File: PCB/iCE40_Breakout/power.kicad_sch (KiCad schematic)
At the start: 18 parts, among them U3 MIC5504-2.5YM5, U4 MIC5504-1.2YM5, U5 MIC5504-3.3YM5, U6 MIC5504-3.3YM5

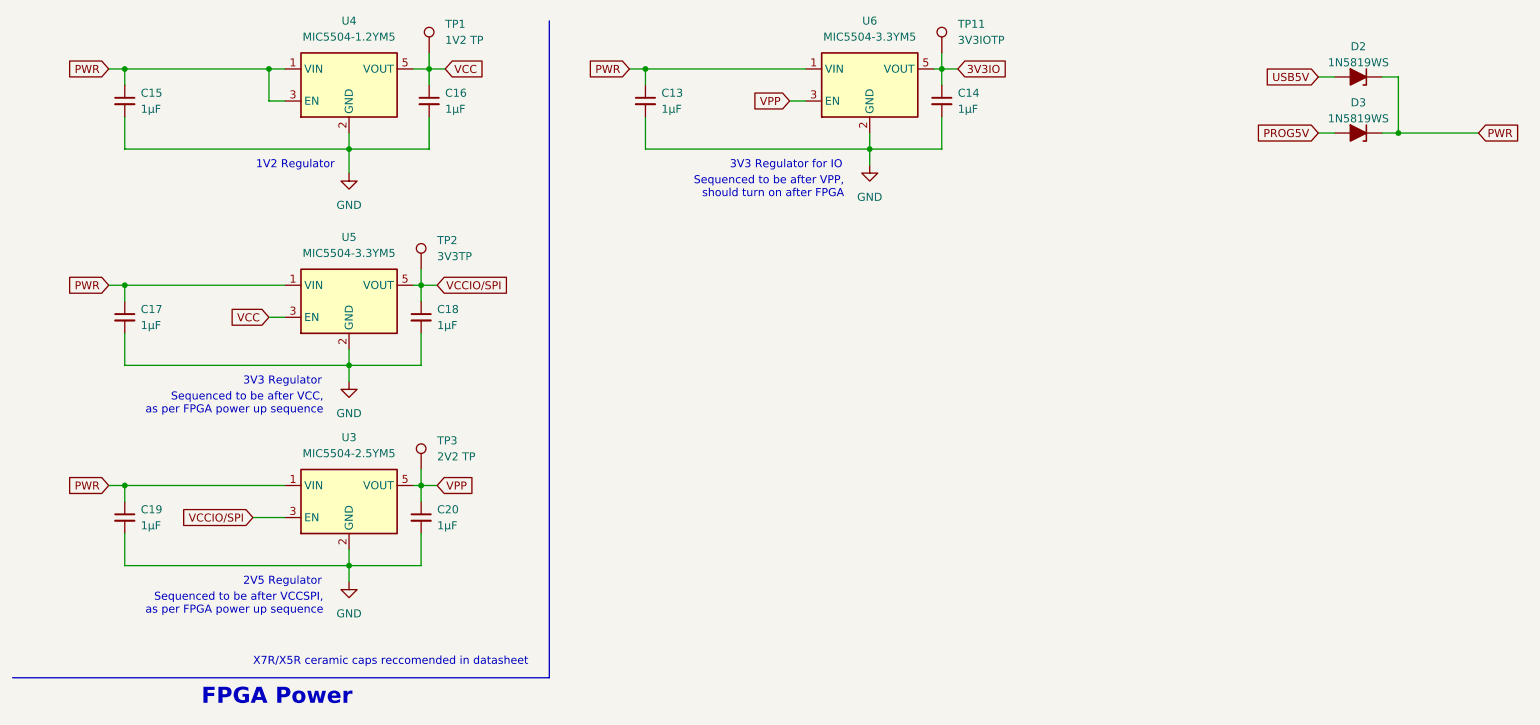
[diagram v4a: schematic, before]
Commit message: Wired FTDI chip to flash memory, and added power connections
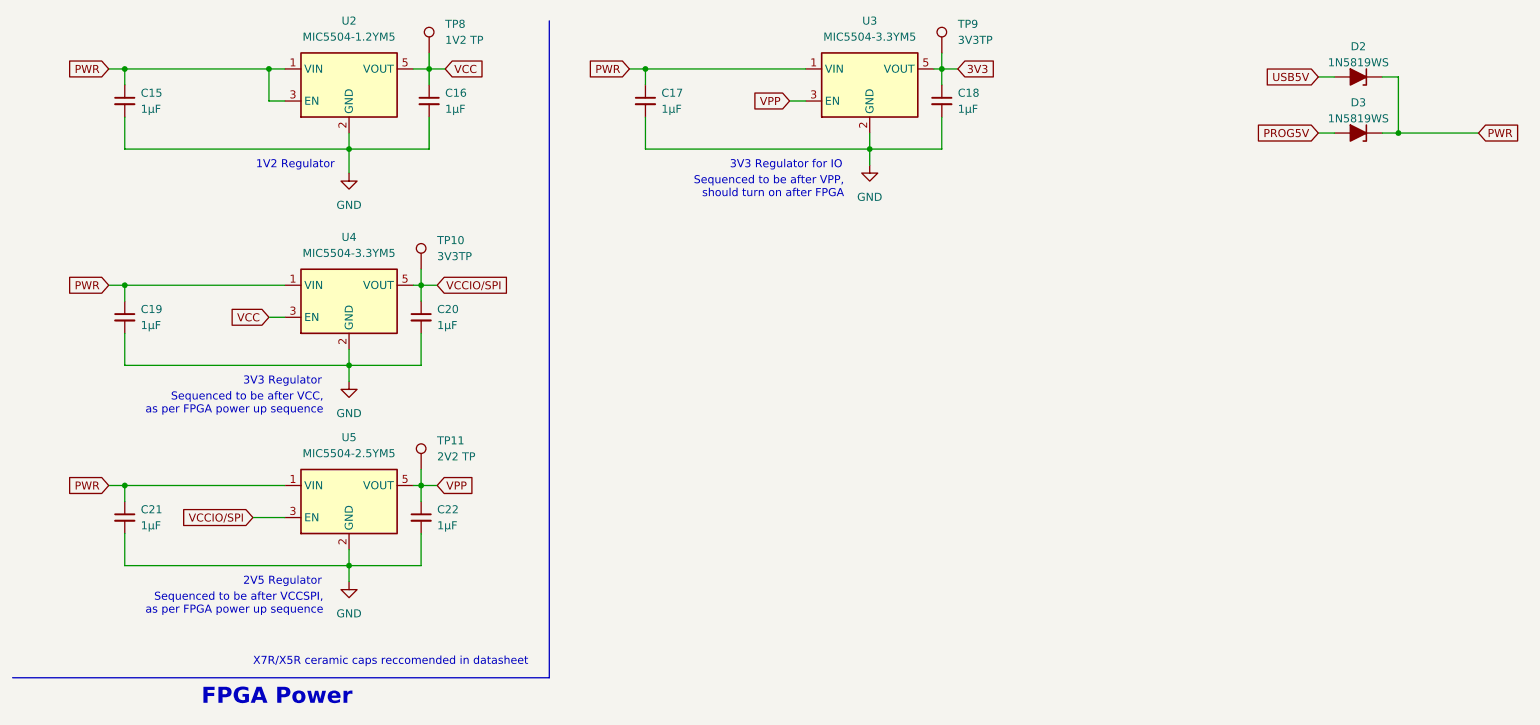
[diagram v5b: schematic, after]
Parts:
- TP9: renamed from TP11; value 3V3IOTP -> 3V3TP
- renumbered C13 to C17, C14 to C18, C17 to C19, C18 to C20, C19 to C21, C20 to C22, TP2 to TP10, TP3 to TP11, TP1 to TP8, U4 to U2, U6 to U3, U5 to U4, U3 to U5
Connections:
- net 3V3IO renamed 3V3
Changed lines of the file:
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@@
 		)
 	)
-	(global_label "3V3IO"
+	(global_label "3V3"
 		(shape input)
 		(at 165.1 21.59 0)
@@
 		(dnp no)
 		(fields_autoplaced yes)
-		(property "Reference" "C20"
+		(property "Reference" "C22"
 			(at 82.55 91.4462 0)
 			(effects
@@
 			(project "iCE40_Breakout"
 				(path "/ce4d7974-ef38-4eea-8119-381c4298ef02/01a0af1d-1c95-48f8-8e55-14d3b3651b87"
-					(reference "C20")
+					(reference "C22")
 					(unit 1)
 				)
@@
 		(dnp no)
 		(fields_autoplaced yes)
-		(property "Reference" "U3"
+		(property "Reference" "U5"
 			(at 68.58 80.01 0)
 			(effects
@@
 			(project "iCE40_Breakout"
 				(path "/ce4d7974-ef38-4eea-8119-381c4298ef02/01a0af1d-1c95-48f8-8e55-14d3b3651b87"
-					(reference "U3")
+					(reference "U5")
 					(unit 1)
 				)
@@
 		(dnp no)
 		(fields_autoplaced yes)
-		(property "Reference" "C18"
+		(property "Reference" "C20"
 			(at 82.55 59.6962 0)
 			(effects
@@
 			(project "iCE40_Breakout"
 				(path "/ce4d7974-ef38-4eea-8119-381c4298ef02/01a0af1d-1c95-48f8-8e55-14d3b3651b87"
-					(reference "C18")
+					(reference "C20")
 					(unit 1)
 				)
@@
 		(on_board yes)
 		(dnp no)
-		(property "Reference" "TP3"
+		(property "Reference" "TP11"
 			(at 82.55 80.5179 0)
 			(effects
@@
 			(project "iCE40_Breakout"
 				(path "/ce4d7974-ef38-4eea-8119-381c4298ef02/01a0af1d-1c95-48f8-8e55-14d3b3651b87"
-					(reference "TP3")
+					(reference "TP11")
 					(unit 1)
 				)
@@
 		(dnp no)
 		(fields_autoplaced yes)
-		(property "Reference" "U4"
+		(property "Reference" "U2"
 			(at 68.58 13.97 0)
 			(effects
@@
 			(project "iCE40_Breakout"
 				(path "/ce4d7974-ef38-4eea-8119-381c4298ef02/01a0af1d-1c95-48f8-8e55-14d3b3651b87"
-					(reference "U4")
+					(reference "U2")
 					(unit 1)
 				)
@@
 		(dnp no)
 		(fields_autoplaced yes)
-		(property "Reference" "C13"
+		(property "Reference" "C17"
 			(at 118.11 25.4062 0)
 			(effects
@@
 			(project "iCE40_Breakout"
 				(path "/ce4d7974-ef38-4eea-8119-381c4298ef02/01a0af1d-1c95-48f8-8e55-14d3b3651b87"
-					(reference "C13")
+					(reference "C17")
 					(unit 1)
 				)
@@
 		(dnp no)
 		(fields_autoplaced yes)
-		(property "Reference" "U5"
+		(property "Reference" "U4"
 			(at 68.58 48.26 0)
 			(effects
@@
 			(project "iCE40_Breakout"
 				(path "/ce4d7974-ef38-4eea-8119-381c4298ef02/01a0af1d-1c95-48f8-8e55-14d3b3651b87"
-					(reference "U5")
+					(reference "U4")
 					(unit 1)
 				)
@@
 		(dnp no)
 		(fields_autoplaced yes)
-		(property "Reference" "#PWR017"
+		(property "Reference" "#PWR020"
 			(at 68.58 44.45 0)
 			(effects
@@
 			(project "iCE40_Breakout"
 				(path "/ce4d7974-ef38-4eea-8119-381c4298ef02/01a0af1d-1c95-48f8-8e55-14d3b3651b87"
-					(reference "#PWR017")
+					(reference "#PWR020")
 					(unit 1)
 				)
@@
 		(on_board yes)
 		(dnp no)
-		(property "Reference" "TP2"
+		(property "Reference" "TP10"
 			(at 82.55 48.7679 0)
 			(effects
@@
 			(project ""
 				(path "/ce4d7974-ef38-4eea-8119-381c4298ef02/01a0af1d-1c95-48f8-8e55-14d3b3651b87"
-					(reference "TP2")
+					(reference "TP10")
 					(unit 1)
 				)
@@
 		(dnp no)
 		(fields_autoplaced yes)
-		(property "Reference" "#PWR019"
+		(property "Reference" "#PWR021"
 			(at 68.58 77.47 0)
 			(effects
@@
 			(project "iCE40_Breakout"
 				(path "/ce4d7974-ef38-4eea-8119-381c4298ef02/01a0af1d-1c95-48f8-8e55-14d3b3651b87"
-					(reference "#PWR019")
+					(reference "#PWR021")
 					(unit 1)
 				)
@@
 		(dnp no)
 		(fields_autoplaced yes)
-		(property "Reference" "#PWR018"
+		(property "Reference" "#PWR022"
 			(at 68.58 109.22 0)
 			(effects
@@
 			(project "iCE40_Breakout"
 				(path "/ce4d7974-ef38-4eea-8119-381c4298ef02/01a0af1d-1c95-48f8-8e55-14d3b3651b87"
-					(reference "#PWR018")
+					(reference "#PWR022")
 					(unit 1)
 				)
@@
 		(dnp no)
 		(fields_autoplaced yes)
-		(property "Reference" "#PWR023"
+		(property "Reference" "#PWR019"
 			(at 151.13 43.18 0)
 			(effects
@@
 			(project "iCE40_Breakout"
 				(path "/ce4d7974-ef38-4eea-8119-381c4298ef02/01a0af1d-1c95-48f8-8e55-14d3b3651b87"
-					(reference "#PWR023")
+					(reference "#PWR019")
 					(unit 1)
 				)
@@
 		(dnp no)
 		(fields_autoplaced yes)
-		(property "Reference" "U6"
+		(property "Reference" "U3"
 			(at 151.13 13.97 0)
 			(effects
@@
 			(project "iCE40_Breakout"
 				(path "/ce4d7974-ef38-4eea-8119-381c4298ef02/01a0af1d-1c95-48f8-8e55-14d3b3651b87"
-					(reference "U6")
+					(reference "U3")
 					(unit 1)
 				)
@@
 		(dnp no)
 		(fields_autoplaced yes)
-		(property "Reference" "C19"
+		(property "Reference" "C21"
 			(at 35.56 91.4462 0)
 			(effects
@@
 			(project "iCE40_Breakout"
 				(path "/ce4d7974-ef38-4eea-8119-381c4298ef02/01a0af1d-1c95-48f8-8e55-14d3b3651b87"
-					(reference "C19")
+					(reference "C21")
 					(unit 1)
 				)
@@
 		(on_board yes)
 		(dnp no)
-		(property "Reference" "TP11"
+		(property "Reference" "TP9"
 			(at 165.1 14.4779 0)
 			(effects
@@
 			)
 		)
-		(property "Value" "3V3IOTP"
+		(property "Value" "3V3TP"
 			(at 165.1 17.0179 0)
 			(effects
@@
 			(project "iCE40_Breakout"
 				(path "/ce4d7974-ef38-4eea-8119-381c4298ef02/01a0af1d-1c95-48f8-8e55-14d3b3651b87"
-					(reference "TP11")
+					(reference "TP9")
 					(unit 1)
 				)
@@
 		(on_board yes)
 		(dnp no)
-		(property "Reference" "TP1"
+		(property "Reference" "TP8"
 			(at 83.82 14.4779 0)
 			(effects
@@
 			(project "iCE40_Breakout"
 				(path "/ce4d7974-ef38-4eea-8119-381c4298ef02/01a0af1d-1c95-48f8-8e55-14d3b3651b87"
-					(reference "TP1")
+					(reference "TP8")
 					(unit 1)
 				)
@@
 		(dnp no)
 		(fields_autoplaced yes)
-		(property "Reference" "C14"
+		(property "Reference" "C18"
 			(at 165.1 25.4062 0)
 			(effects
@@
 			(project "iCE40_Breakout"
 				(path "/ce4d7974-ef38-4eea-8119-381c4298ef02/01a0af1d-1c95-48f8-8e55-14d3b3651b87"
-					(reference "C14")
+					(reference "C18")
 					(unit 1)
 				)
@@
 		(dnp no)
 		(fields_autoplaced yes)
-		(property "Reference" "C17"
+		(property "Reference" "C19"
 			(at 35.56 59.6962 0)
 			(effects
@@
 			(project "iCE40_Breakout"
 				(path "/ce4d7974-ef38-4eea-8119-381c4298ef02/01a0af1d-1c95-48f8-8e55-14d3b3651b87"
-					(reference "C17")
-					(unit 1)
-				)
+					(reference "C19")
+					(unit 1)
+				)

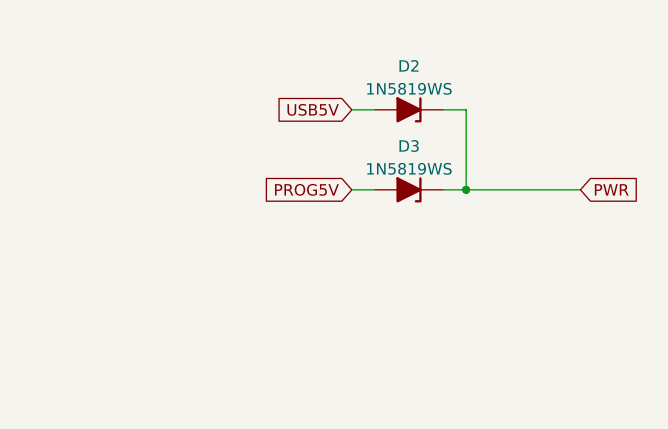
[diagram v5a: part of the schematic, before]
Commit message: Added sheet information, and fixed ERC errors
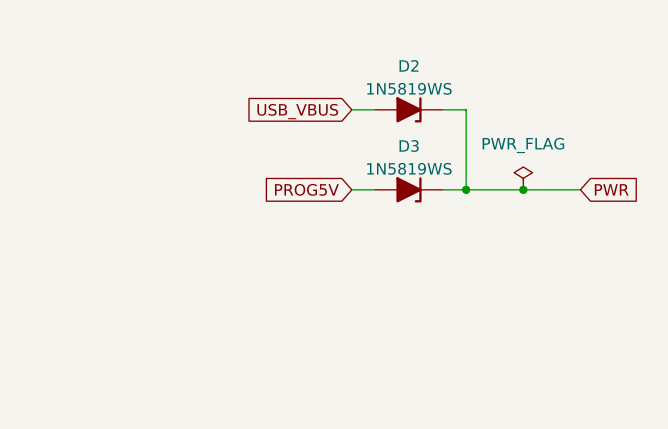
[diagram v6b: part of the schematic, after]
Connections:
- net USB5V renamed USB_VBUS
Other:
- company: (none) -> S3I
- title: (none) -> iCE40 Breakout
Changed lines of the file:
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@@
 	(generator_version "9.0")
 	(paper "A4")
+	(title_block
+		(title "iCE40 Breakout")
+		(date "2025-11-26")
+		(rev "V1R0")
+		(company "S3I")
+		(comment 1 "Voltage regulators")
+	)
 	(text "1V2 Regulator"
 		(exclude_from_sim no)
@@
 	)
 	(junction
+		(at 241.3 31.75)
+		(diameter 0)
+		(color 0 0 0 0)
+	)
+	(junction
 		(at 33.02 21.59)
 		(diameter 0)
@@
 	(wire
 		(pts
+			(xy 241.3 31.75) (xy 247.65 31.75)
+		)
+		(stroke
+			(width 0)
+			(type default)
+		)
+	)
+	(wire
+		(pts
 			(xy 78.74 21.59) (xy 81.28 21.59)
 		)
@@
 	(wire
 		(pts
-			(xy 234.95 31.75) (xy 247.65 31.75)
+			(xy 234.95 31.75) (xy 241.3 31.75)
 		)
 		(stroke
@@
 		)
 	)
+	(global_label "USB_VBUS"
+		(shape input)
+		(at 222.25 22.86 180)
+		(fields_autoplaced yes)
+		(effects
+			(font
+				(size 1.27 1.27)
+			)
+			(justify right)
+		)
+		(property "Intersheetrefs" "${INTERSHEET_REFS}"
+			(at 209.5886 22.86 0)
+			(effects
+				(font
+					(size 1.27 1.27)
+				)
+				(justify right)
+				(hide yes)
+			)
+		)
+	)
 	(global_label "VCCIO{slash}SPI"
 		(shape input)
@@
 				)
 				(justify left)
-				(hide yes)
-			)
-		)
-	)
-	(global_label "USB5V"
-		(shape input)
-		(at 222.25 22.86 180)
-		(fields_autoplaced yes)
-		(effects
-			(font
-				(size 1.27 1.27)
-			)
-			(justify right)
-		)
-		(property "Intersheetrefs" "${INTERSHEET_REFS}"
-			(at 213.1567 22.86 0)
-			(effects
-				(font
-					(size 1.27 1.27)
-				)
-				(justify right)
 				(hide yes)
 			)
@@
 	)
 	(symbol
+		(lib_id "power:PWR_FLAG")
+		(at 241.3 31.75 0)
+		(unit 1)
+		(exclude_from_sim no)
+		(in_bom yes)
+		(on_board yes)
+		(dnp no)
+		(fields_autoplaced yes)
+		(property "Reference" "#FLG02"
+			(at 241.3 29.845 0)
+			(effects
+				(font
+					(size 1.27 1.27)
+				)
+				(hide yes)
+			)
+		)
+		(property "Value" "PWR_FLAG"
+			(at 241.3 26.67 0)
+			(effects
+				(font
+					(size 1.27 1.27)
+				)
+			)
+		)
+		(property "Footprint" ""
+			(at 241.3 31.75 0)
+			(effects
+				(font
+					(size 1.27 1.27)
+				)
+				(hide yes)
+			)
+		)
+		(property "Datasheet" "~"
+			(at 241.3 31.75 0)
+			(effects
+				(font
+					(size 1.27 1.27)
+				)
+				(hide yes)
+			)
+		)
+		(property "Description" "Special symbol for telling ERC where power comes from"
+			(at 241.3 31.75 0)
+			(effects
+				(font
+					(size 1.27 1.27)
+				)
+				(hide yes)
+			)
+		)
+		(pin "1"
+		)
+		(instances
+			(project "iCE40_Breakout"
+				(path "/ce4d7974-ef38-4eea-8119-381c4298ef02/01a0af1d-1c95-48f8-8e55-14d3b3651b87"
+					(reference "#FLG02")
+					(unit 1)
+				)
+			)
+		)
+	)
+	(symbol
 		(lib_id "Connector:TestPoint")
 		(at 80.01 85.09 0)
@@
 		(dnp no)
 		(fields_autoplaced yes)
-		(property "Reference" "#PWR020"
+		(property "Reference" "#PWR023"
 			(at 68.58 44.45 0)
 			(effects
@@
 			(project "iCE40_Breakout"
 				(path "/ce4d7974-ef38-4eea-8119-381c4298ef02/01a0af1d-1c95-48f8-8e55-14d3b3651b87"
-					(reference "#PWR020")
+					(reference "#PWR023")
 					(unit 1)
 				)
@@
 		(dnp no)
 		(fields_autoplaced yes)
-		(property "Reference" "#PWR021"
+		(property "Reference" "#PWR024"
 			(at 68.58 77.47 0)
 			(effects
@@
 			(project "iCE40_Breakout"
 				(path "/ce4d7974-ef38-4eea-8119-381c4298ef02/01a0af1d-1c95-48f8-8e55-14d3b3651b87"
-					(reference "#PWR021")
+					(reference "#PWR024")
 					(unit 1)
 				)
@@
 		(dnp no)
 		(fields_autoplaced yes)
-		(property "Reference" "#PWR022"
+		(property "Reference" "#PWR025"
 			(at 68.58 109.22 0)
 			(effects
@@
 		(property "Description" "Power symbol creates a global label with name \"GND\" , ground"
 			(at 68.58 102.87 0)
+			(effects
+				(font
+					(size 1.27 1.27)
+				)
+				(hide yes)
+			)
+		)
+		(pin "1"
+		)
+		(instances
+			(project "iCE40_Breakout"
+				(path "/ce4d7974-ef38-4eea-8119-381c4298ef02/01a0af1d-1c95-48f8-8e55-14d3b3651b87"
+					(reference "#PWR025")
+					(unit 1)
+				)
+			)
+		)
+	)
+	(symbol
+		(lib_id "power:GND")
+		(at 151.13 36.83 0)
+		(unit 1)
+		(exclude_from_sim no)
+		(in_bom yes)
+		(on_board yes)
+		(dnp no)
+		(fields_autoplaced yes)
+		(property "Reference" "#PWR022"
+			(at 151.13 43.18 0)
+			(effects
+				(font
+					(size 1.27 1.27)
+				)
+				(hide yes)
+			)
+		)
+		(property "Value" "GND"
+			(at 151.13 41.91 0)
+			(effects
+				(font
+					(size 1.27 1.27)
+				)
+			)
+		)
+		(property "Footprint" ""
+			(at 151.13 36.83 0)
+			(effects
+				(font
+					(size 1.27 1.27)
+				)
+				(hide yes)
+			)
+		)
+		(property "Datasheet" ""
+			(at 151.13 36.83 0)
+			(effects
+				(font
+					(size 1.27 1.27)
+				)
+				(hide yes)
+			)
+		)
+		(property "Description" "Power symbol creates a global label with name \"GND\" , ground"
+			(at 151.13 36.83 0)
 			(effects
 				(font
@@
 					(unit 1)
 				)
-			)
-		)
-	)
-	(symbol
-		(lib_id "power:GND")
-		(at 151.13 36.83 0)
-		(unit 1)
-		(exclude_from_sim no)
-		(in_bom yes)
-		(on_board yes)
-		(dnp no)
-		(fields_autoplaced yes)
-		(property "Reference" "#PWR019"
-			(at 151.13 43.18 0)
-			(effects
-				(font
-					(size 1.27 1.27)
-				)
-				(hide yes)
-			)
-		)
-		(property "Value" "GND"
-			(at 151.13 41.91 0)
-			(effects
-				(font
-					(size 1.27 1.27)
-				)
-			)
-		)
-		(property "Footprint" ""
-			(at 151.13 36.83 0)
-			(effects
-				(font
-					(size 1.27 1.27)
-				)
-				(hide yes)
-			)
-		)
-		(property "Datasheet" ""
-			(at 151.13 36.83 0)
-			(effects
-				(font
-					(size 1.27 1.27)
-				)
-				(hide yes)
-			)
-		)
-		(property "Description" "Power symbol creates a global label with name \"GND\" , ground"
-			(at 151.13 36.83 0)
-			(effects
-				(font
-					(size 1.27 1.27)
-				)
-				(hide yes)
-			)
-		)
-		(pin "1"
-		)
-		(instances
-			(project "iCE40_Breakout"
-				(path "/ce4d7974-ef38-4eea-8119-381c4298ef02/01a0af1d-1c95-48f8-8e55-14d3b3651b87"
-					(reference "#PWR019")
-					(unit 1)
-				)

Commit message: Updated all TPs to use pads, not holes for hooks. Also removed duplicate SPI programming TPs
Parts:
- TP10, TP11, TP8, TP9: footprint TestPoint:TestPoint_Loop_D1.80mm_Drill1.0mm_Beaded -> TestPoint:TestPoint_Pad_D1.0mm
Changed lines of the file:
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@@
 			)
 		)
-		(property "Footprint" "TestPoint:TestPoint_Loop_D1.80mm_Drill1.0mm_Beaded"
+		(property "Footprint" "TestPoint:TestPoint_Pad_D1.0mm"
 			(at 85.09 85.09 0)
 			(effects
@@
 			)
 		)
-		(property "Footprint" "TestPoint:TestPoint_Loop_D1.80mm_Drill1.0mm_Beaded"
+		(property "Footprint" "TestPoint:TestPoint_Pad_D1.0mm"
 			(at 85.09 53.34 0)
 			(effects
@@
 			)
 		)
-		(property "Footprint" "TestPoint:TestPoint_Loop_D1.80mm_Drill1.0mm_Beaded"
+		(property "Footprint" "TestPoint:TestPoint_Pad_D1.0mm"
 			(at 167.64 19.05 0)
 			(effects
@@
 			)
 		)
-		(property "Footprint" "TestPoint:TestPoint_Loop_D1.80mm_Drill1.0mm_Beaded"
+		(property "Footprint" "TestPoint:TestPoint_Pad_D1.0mm"
 			(at 86.36 19.05 0)
 			(effects

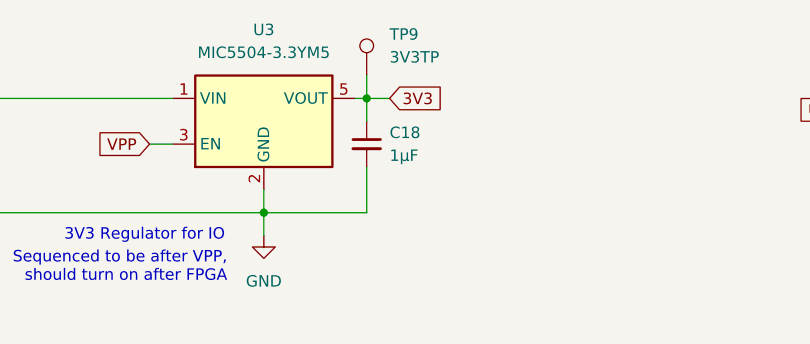
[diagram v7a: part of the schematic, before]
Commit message: Initial layout of all components
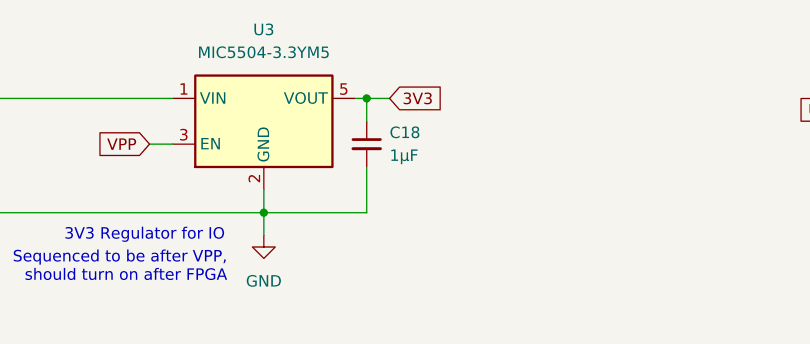
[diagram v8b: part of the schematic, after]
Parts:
- removed TP9: 3V3TP, TestPoint:TestPoint_Pad_D1.0mm, symbol Connector:TestPoint
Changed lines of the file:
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@@
-	(wire
-		(pts
-			(xy 162.56 19.05) (xy 162.56 21.59)
-		)
-		(stroke
-			(width 0)
-			(type default)
-		)
-	)
 	(wire
 		(pts
@@
 					(unit 1)
 				)
-			)
-		)
-	)
-	(symbol
-		(lib_id "Connector:TestPoint")
-		(at 162.56 19.05 0)
-		(unit 1)
-		(exclude_from_sim no)
-		(in_bom yes)
-		(on_board yes)
-		(dnp no)
-		(property "Reference" "TP9"
-			(at 165.1 14.4779 0)
-			(effects
-				(font
-					(size 1.27 1.27)
-				)
-				(justify left)
-			)
-		)
-		(property "Value" "3V3TP"
-			(at 165.1 17.0179 0)
-			(effects
-				(font
-					(size 1.27 1.27)
-				)
-				(justify left)
-			)
-		)
-		(property "Footprint" "TestPoint:TestPoint_Pad_D1.0mm"
-			(at 167.64 19.05 0)
-			(effects
-				(font
-					(size 1.27 1.27)
-				)
-				(hide yes)
-			)
-		)
-		(property "Datasheet" "~"
-			(at 167.64 19.05 0)
-			(effects
-				(font
-					(size 1.27 1.27)
-				)
-				(hide yes)
-			)
-		)
-		(property "Description" "test point"
-			(at 162.56 19.05 0)
-			(effects
-				(font
-					(size 1.27 1.27)
-				)
-				(hide yes)
-			)
-		)
-		(pin "1"
-		)
-		(instances
-			(project "iCE40_Breakout"
-				(path "/ce4d7974-ef38-4eea-8119-381c4298ef02/01a0af1d-1c95-48f8-8e55-14d3b3651b87"
-					(reference "TP9")
-					(unit 1)
-				)
